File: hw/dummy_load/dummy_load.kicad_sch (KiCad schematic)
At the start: 47 parts, among them Q10 DMG2305UX-7, U1 LM358, U2 AD620, U21 LM4040B30FTA, U3 LM4040B30FTA, U5 74HC4051, U6 AD5272BCP, U7 AD5272BCP, U8 AMS1117-5.0

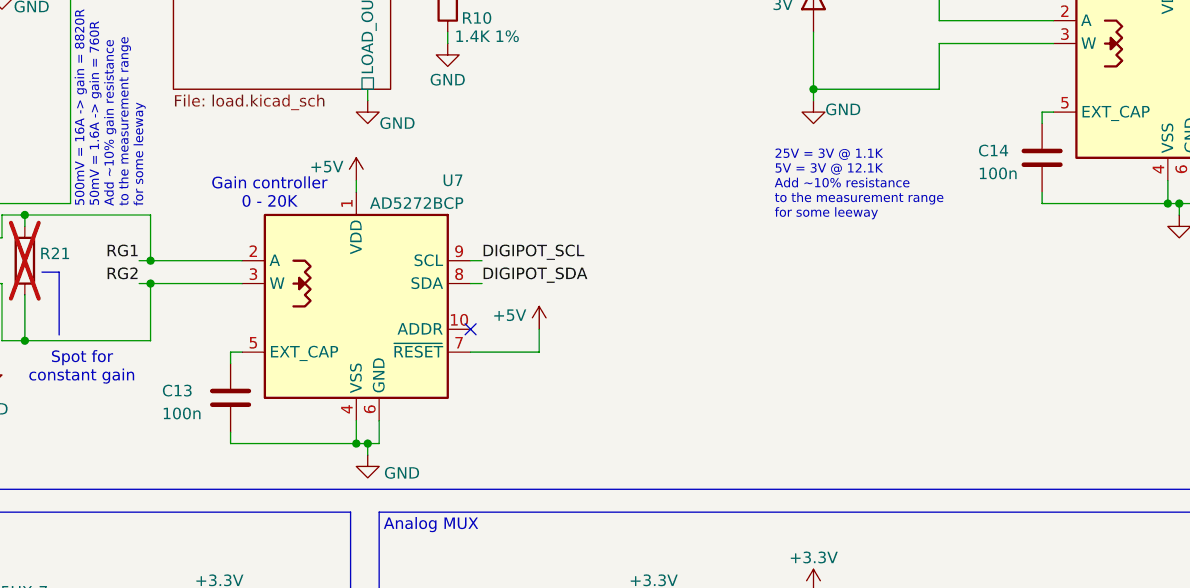
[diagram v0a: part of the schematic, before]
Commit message: Fix digipot cap value
Signed-off-by: Mateusz Pajak <22417805+Tai-Min@users.noreply.github.com>
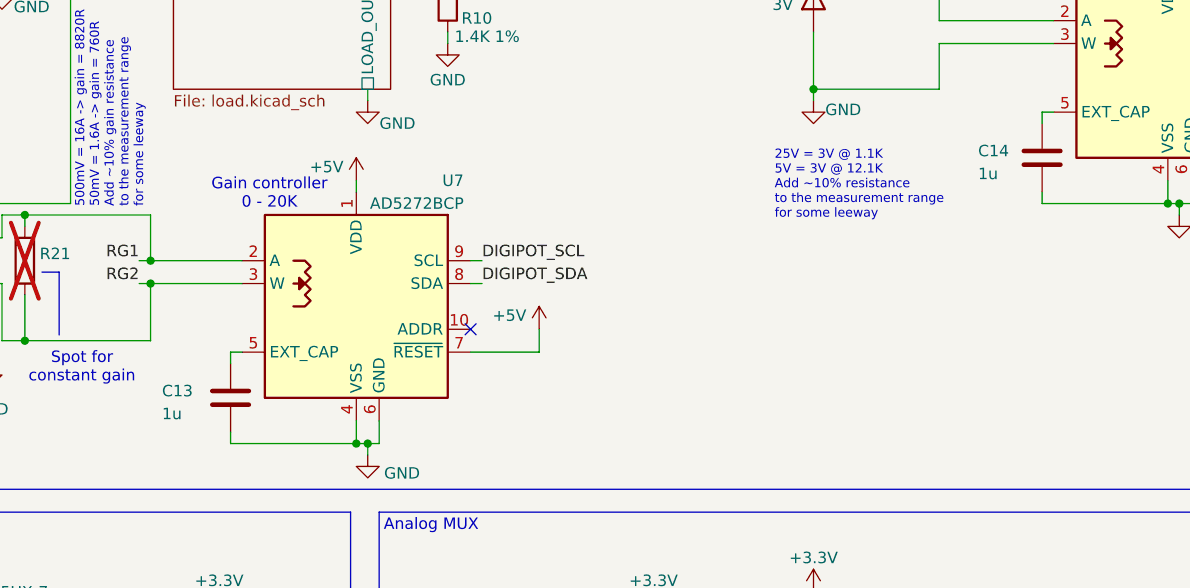
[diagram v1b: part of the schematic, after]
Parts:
- C13, C14: value 100n -> 1u; LCSC Part # C24497 -> C1848
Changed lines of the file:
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@@
 			)
 		)
-		(property "Value" "100n"
+		(property "Value" "1u"
 			(at 227.838 57.658 0)
 			(effects
@@
 			)
 		)
-		(property "LCSC Part #" "C24497"
+		(property "LCSC Part #" "C1848"
 			(at 234.95 55.88 0)
 			(effects
@@
 			)
 		)
-		(property "Value" "100n"
+		(property "Value" "1u"
 			(at 137.16 84.328 0)
 			(effects
@@
 			)
 		)
-		(property "LCSC Part #" "C24497"
+		(property "LCSC Part #" "C1848"
 			(at 144.78 82.55 0)
 			(effects

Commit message: Better PCB design, update BOM, add UART header for debugging (#7)
Signed-off-by: Mateusz Pajak <22417805+Tai-Min@users.noreply.github.com>
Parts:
- added H2: MountingHole, MountingHole:MountingHole_3.2mm_M3_Pad_Via, symbol Mechanical:MountingHole
- C1, C4, C8: footprint Capacitor_SMD:C_1206_3216Metric_Pad1.33x1.80mm_HandSolder -> Capacitor_SMD:C_0603_1608Metric; LCSC Part # C24497 -> C14663
- C13, C14, C15, C2, C3, C9: footprint Capacitor_SMD:C_1206_3216Metric_Pad1.33x1.80mm_HandSolder -> Capacitor_SMD:C_0603_1608Metric; LCSC Part # C1848 -> C15849
- C5: footprint Capacitor_SMD:C_1206_3216Metric_Pad1.33x1.80mm_HandSolder -> Capacitor_SMD:C_1206_3216Metric
- C6, C7: footprint Capacitor_SMD:C_1206_3216Metric_Pad1.33x1.80mm_HandSolder -> Capacitor_SMD:C_0603_1608Metric
- Q10: footprint Package_TO_SOT_SMD:SC-59_Handsoldering -> Package_TO_SOT_SMD:SC-59
- R1, R2: footprint Resistor_SMD:R_1206_3216Metric_Pad1.30x1.75mm_HandSolder -> Resistor_SMD:R_0603_1608Metric; LCSC Part # C2907469 -> C22978
- R10: footprint Resistor_SMD:R_1206_3216Metric_Pad1.30x1.75mm_HandSolder -> Resistor_SMD:R_0603_1608Metric; LCSC Part # C5713320 -> C25957
- R11, R12, R13, R15, R5: footprint Resistor_SMD:R_1206_3216Metric_Pad1.30x1.75mm_HandSolder -> Resistor_SMD:R_0603_1608Metric; LCSC Part # C17902 -> C98220
- R16: footprint Resistor_SMD:R_1206_3216Metric_Pad1.30x1.75mm_HandSolder -> Resistor_SMD:R_0603_1608Metric; LCSC Part # C18012 -> C2907033
- R21, R7: footprint Resistor_SMD:R_1206_3216Metric_Pad1.30x1.75mm_HandSolder -> Resistor_SMD:R_0603_1608Metric
- R22, R23: footprint Resistor_SMD:R_1206_3216Metric_Pad1.30x1.75mm_HandSolder -> Resistor_SMD:R_0603_1608Metric; LCSC Part # C17936 -> C99782
- R3, R9: footprint Resistor_SMD:R_1206_3216Metric_Pad1.30x1.75mm_HandSolder -> Resistor_SMD:R_0603_1608Metric; LCSC Part # C136889 -> C98220
- R4: footprint Resistor_SMD:R_1206_3216Metric_Pad1.30x1.75mm_HandSolder -> Resistor_SMD:R_0603_1608Metric; LCSC Part # C706405 -> C22548
- R6: value 8.06K -> 8.06K 1%; footprint Resistor_SMD:R_1206_3216Metric_Pad1.30x1.75mm_HandSolder -> Resistor_SMD:R_0603_1608Metric; LCSC Part # C3017010 -> C23112
- R72: footprint Resistor_SMD:R_1206_3216Metric_Pad1.30x1.75mm_HandSolder -> Resistor_SMD:R_0603_1608Metric; LCSC Part # C2930418 -> C8218
- R8: footprint Resistor_SMD:R_1206_3216Metric_Pad1.30x1.75mm_HandSolder -> Resistor_SMD:R_0603_1608Metric; LCSC Part # C2907440 -> C22548
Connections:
- net NTC_HEATSINK_3 is gone; now on net NTC_HEATSINK_1: U5.14 (A1)
- net NTC_HEATSINK_4 is gone; now on an unnamed net: U5.13 (A0)
- net DUT_SENSE: now also U5.12 (A3); no longer U5.5 (A5)
- net DUT_SENSE_PRECISE: now also A1.32 (GPIO27_ADC1); no longer A1.34 (GPIO28_ADC2)
- net GND: now also H1.1, H3.1, H4.1, H2.1; no longer A1.33 (AGND), C1.1, C2.1, C3.1, C4.1, C8.1, C9.1, D1.2 (A), D3.2 (A), D5.2 (A), R10.1, R16.1, R3.1, R5.1, U1.4 (V-), U2.2 (-), U2.4 (Vs-), U2.5 (Ref), U21.2 (A), U3.2 (A), U5.7 (VEE), U6.3 (W)
- net LOAD_CTRL: now also A1.29 (GPIO22); no longer A1.26 (GPIO20)
- net LOAD_FEEDBACK: now also A1.34 (GPIO28_ADC2); no longer A1.32 (GPIO27_ADC1)
- net MUX_S0: now also A1.24 (GPIO18); no longer A1.21 (GPIO16)
- net MUX_S2: now also A1.21 (GPIO16); no longer A1.24 (GPIO18)
- net NTC_AMBIENT: now also U5.1 (A4); no longer U5.2 (A6)
- net NTC_DUT: now also U5.2 (A6); no longer U5.1 (A4)
- net NTC_HEATSINK_1: no longer U5.4 (A7)
- net at C9.2, R15.1, R16.2: no longer U5.12 (A3)
- net UART_TX: now reaches A1.6 (GPIO4)
- net UART_RX: now reaches A1.7 (GPIO5)
- new net GNDA: A1.33 (AGND), C1.1, C2.1, C3.1, C4.1, C8.1, C9.1, D1.2 (A), D3.2 (A), D5.2 (A), R10.1, R16.1, R3.1, R5.1, U1.4 (V-), U2.2 (-), U2.4 (Vs-), U2.5 (Ref), U21.2 (A), U3.2 (A), U5.7 (VEE), U6.3 (W)
- new net NTC_SPARE_1: U5.4 (A7)
- new net NTC_SPARE_2: U5.5 (A5)
- no-connect marks 19 -> 17
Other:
- sheet connectors ports: added NTC_SPARE_1, NTC_SPARE_2, UART_RX, UART_TX; removed NTC_HEATSINK_3, NTC_HEATSINK_4
- moved on the sheet: C15, C5, R72, U21, U8
